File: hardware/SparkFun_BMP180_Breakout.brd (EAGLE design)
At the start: 15.2 x 15.2 mm, 16 parts, among them U1 BMP180

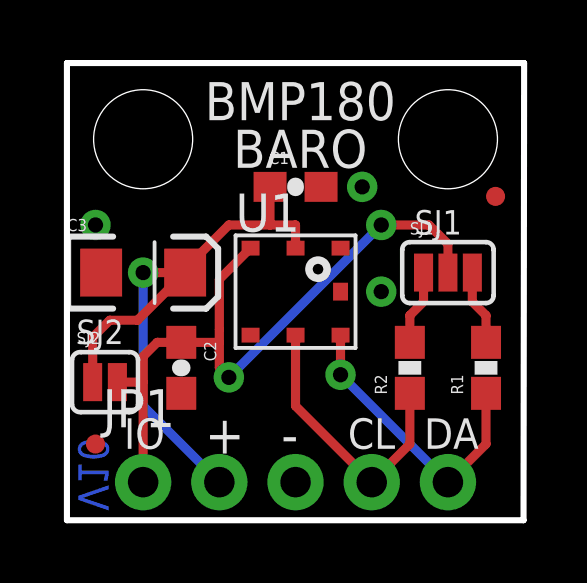
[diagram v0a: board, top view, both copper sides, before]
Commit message: Version 2.0, initial commit
Rerouted connector for new standard I2C pinout.
Cleaned up layout and schematic per standards.
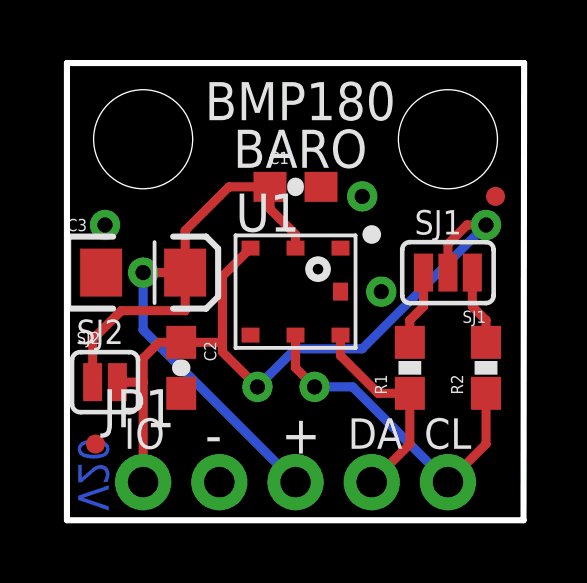
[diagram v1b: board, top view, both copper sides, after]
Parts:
- removed LOGO1: LOGO-SFENW2, SparkFun-Aesthetics:SFE-NEW-WEB
- added LOGO3: SFE_LOGO_NAME.1_INCH, SparkFun-Aesthetics:SFE_LOGO_NAME_.1
- moved R1 2.54 mm to (11.4, 5.08)
- moved R2 2.54 mm to (14.0, 5.08)
- turned SJ1 to 180 degrees
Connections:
- net GND: now also JP1.2; no longer JP1.3
- net SCL: now also JP1.5; no longer JP1.4
- net SDA: now also JP1.4; no longer JP1.5
- net VDD: now also JP1.3; no longer JP1.2
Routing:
- net SDA: track 9.87 -> 7.00 mm, vias 1 -> 0
- net VDD: track 21.4 -> 23.9 mm
- net VDDIO: track 23.3 -> 25.7 mm
- net SCL: track 9.44 -> 11.2 mm, vias 0 -> 1
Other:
- board text added: "V20"
- board text removed: "V10"
